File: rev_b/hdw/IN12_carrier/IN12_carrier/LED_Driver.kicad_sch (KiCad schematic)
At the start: 27 parts, among them U2101 LP5009

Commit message: lots of routing and design progress on IN12 carrier board
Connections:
- net +3V3 renamed +3.3V
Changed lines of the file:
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@@
     )
   )
-  (symbol (lib_id "Analog_Clock-rescue:+3.3V-power") (at 233.68 62.23 0) (unit 1)
+  (symbol (lib_id "power:+3.3V") (at 233.68 62.23 0) (unit 1)
     (in_bom yes) (on_board yes) (dnp no)
     (property "Reference" "#PWR01819" (at 233.68 66.04 0)
@@
     )
   )
-  (symbol (lib_id "Analog_Clock-rescue:+3.3V-power") (at 85.344 146.304 0) (unit 1)
+  (symbol (lib_id "power:+3.3V") (at 85.344 146.304 0) (unit 1)
     (in_bom yes) (on_board yes) (dnp no)
     (property "Reference" "#PWR?" (at 85.344 150.114 0)
@@
     )
   )
-  (symbol (lib_id "Analog_Clock-rescue:+3.3V-power") (at 104.394 146.304 0) (unit 1)
+  (symbol (lib_id "power:+3.3V") (at 104.394 146.304 0) (unit 1)
     (in_bom yes) (on_board yes) (dnp no)
     (property "Reference" "#PWR?" (at 104.394 150.114 0)
@@
     )
   )
-  (symbol (lib_id "Analog_Clock-rescue:+3.3V-power") (at 83.82 115.57 90) (unit 1)
+  (symbol (lib_id "power:+3.3V") (at 83.82 115.57 90) (unit 1)
     (in_bom yes) (on_board yes) (dnp no)
     (property "Reference" "#PWR02108" (at 87.63 115.57 0)
@@
     )
   )
-  (symbol (lib_id "Analog_Clock-rescue:+3.3V-power") (at 104.14 24.13 0) (unit 1)
+  (symbol (lib_id "power:+3.3V") (at 104.14 24.13 0) (unit 1)
     (in_bom yes) (on_board yes) (dnp no)
     (property "Reference" "#PWR?" (at 104.14 27.94 0)
@@
     )
   )
-  (symbol (lib_id "Analog_Clock-rescue:+3.3V-power") (at 93.98 100.33 0) (unit 1)
+  (symbol (lib_id "power:+3.3V") (at 93.98 100.33 0) (unit 1)
     (in_bom yes) (on_board yes) (dnp no)
     (property "Reference" "#PWR02108" (at 93.98 104.14 0)
@@
     )
   )
-  (symbol (lib_id "Analog_Clock-rescue:+3.3V-power") (at 154.94 29.21 0) (unit 1)
+  (symbol (lib_id "power:+3.3V") (at 154.94 29.21 0) (unit 1)
     (in_bom yes) (on_board yes) (dnp no)
     (property "Reference" "#PWR01819" (at 154.94 33.02 0)
@@
     )
   )
-  (symbol (lib_id "Analog_Clock-rescue:+3.3V-power") (at 233.68 29.21 0) (unit 1)
+  (symbol (lib_id "power:+3.3V") (at 233.68 29.21 0) (unit 1)
     (in_bom yes) (on_board yes) (dnp no)
     (property "Reference" "#PWR01819" (at 233.68 33.02 0)
@@
     )
   )
-  (symbol (lib_id "Analog_Clock-rescue:+3.3V-power") (at 93.98 161.29 0) (unit 1)
+  (symbol (lib_id "power:+3.3V") (at 93.98 161.29 0) (unit 1)
     (in_bom yes) (on_board yes) (dnp no)
     (property "Reference" "#PWR02108" (at 93.98 165.1 0)
@@
     )
   )
-  (symbol (lib_id "Analog_Clock-rescue:+3.3V-power") (at 194.31 62.23 0) (unit 1)
+  (symbol (lib_id "power:+3.3V") (at 194.31 62.23 0) (unit 1)
     (in_bom yes) (on_board yes) (dnp no)
     (property "Reference" "#PWR01819" (at 194.31 66.04 0)
@@
     )
   )
-  (symbol (lib_id "Analog_Clock-rescue:+3.3V-power") (at 93.98 39.37 0) (unit 1)
+  (symbol (lib_id "power:+3.3V") (at 93.98 39.37 0) (unit 1)
     (in_bom yes) (on_board yes) (dnp no)
     (property "Reference" "#PWR02108" (at 93.98 43.18 0)
@@
     )
   )
-  (symbol (lib_id "Analog_Clock-rescue:+3.3V-power") (at 85.344 85.344 0) (unit 1)
+  (symbol (lib_id "power:+3.3V") (at 85.344 85.344 0) (unit 1)
     (in_bom yes) (on_board yes) (dnp no)
     (property "Reference" "#PWR?" (at 85.344 89.154 0)
@@
     )
   )
-  (symbol (lib_id "Analog_Clock-rescue:+3.3V-power") (at 154.94 62.23 0) (unit 1)
+  (symbol (lib_id "power:+3.3V") (at 154.94 62.23 0) (unit 1)
     (in_bom yes) (on_board yes) (dnp no)
     (property "Reference" "#PWR01819" (at 154.94 66.04 0)
@@
     )
   )
-  (symbol (lib_id "Analog_Clock-rescue:+3.3V-power") (at 154.94 100.33 0) (unit 1)
+  (symbol (lib_id "power:+3.3V") (at 154.94 100.33 0) (unit 1)
     (in_bom yes) (on_board yes) (dnp no)
     (property "Reference" "#PWR01819" (at 154.94 104.14 0)
@@
     )
   )
-  (symbol (lib_id "Analog_Clock-rescue:+3.3V-power") (at 194.31 100.33 0) (unit 1)
+  (symbol (lib_id "power:+3.3V") (at 194.31 100.33 0) (unit 1)
     (in_bom yes) (on_board yes) (dnp no)
     (property "Reference" "#PWR01819" (at 194.31 104.14 0)
@@
     )
   )
-  (symbol (lib_id "Analog_Clock-rescue:+3.3V-power") (at 85.09 24.13 0) (unit 1)
+  (symbol (lib_id "power:+3.3V") (at 85.09 24.13 0) (unit 1)
     (in_bom yes) (on_board yes) (dnp no)
     (property "Reference" "#PWR?" (at 85.09 27.94 0)
@@
     )
   )
-  (symbol (lib_id "Analog_Clock-rescue:+3.3V-power") (at 83.82 179.07 90) (unit 1)
+  (symbol (lib_id "power:+3.3V") (at 83.82 179.07 90) (unit 1)
     (in_bom yes) (on_board yes) (dnp no)
     (property "Reference" "#PWR02108" (at 87.63 179.07 0)
@@
     )
   )
-  (symbol (lib_id "Analog_Clock-rescue:+3.3V-power") (at 194.31 29.21 0) (unit 1)
+  (symbol (lib_id "power:+3.3V") (at 194.31 29.21 0) (unit 1)
     (in_bom yes) (on_board yes) (dnp no)
     (property "Reference" "#PWR01819" (at 194.31 33.02 0)
@@
     )
   )
-  (symbol (lib_id "Analog_Clock-rescue:+3.3V-power") (at 104.394 85.344 0) (unit 1)
+  (symbol (lib_id "power:+3.3V") (at 104.394 85.344 0) (unit 1)
     (in_bom yes) (on_board yes) (dnp no)
     (property "Reference" "#PWR?" (at 104.394 89.154 0)

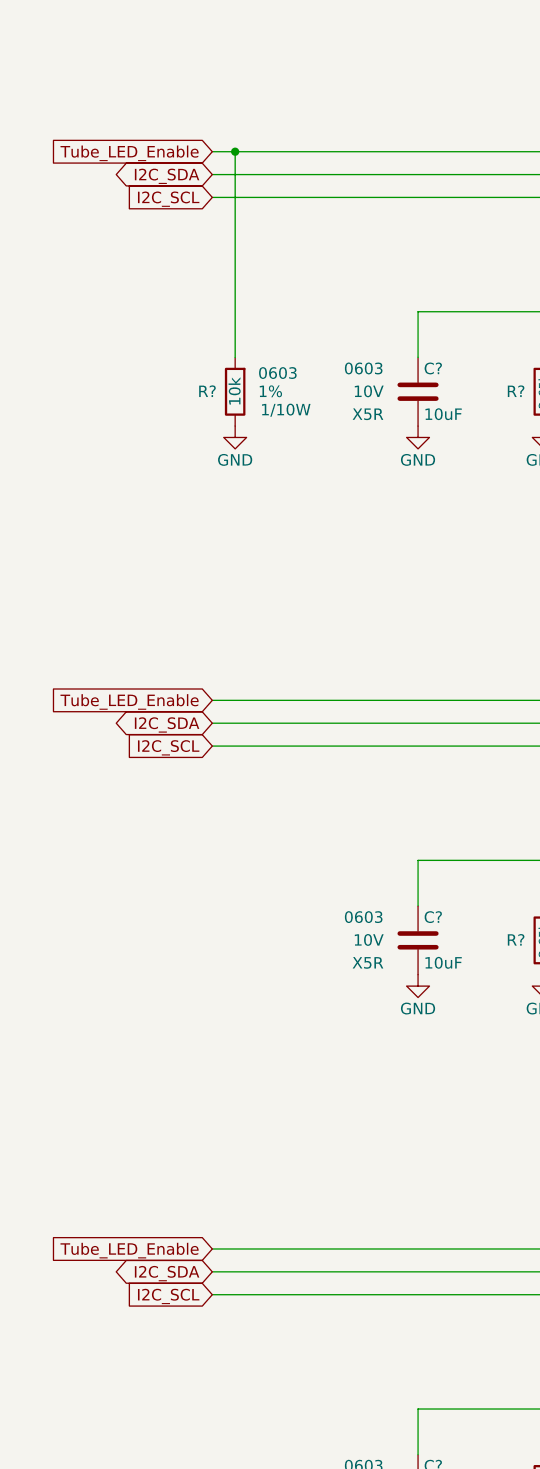
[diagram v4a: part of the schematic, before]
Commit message: got IN12 carrier board unconnects to 0
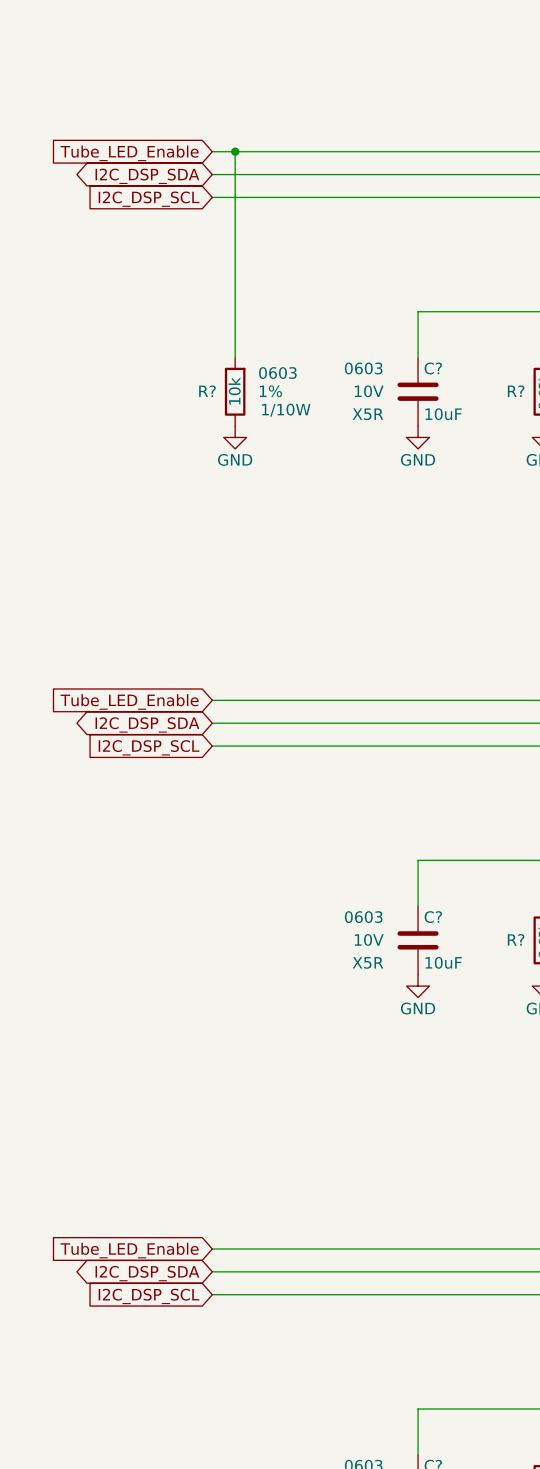
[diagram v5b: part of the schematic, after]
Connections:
- net I2C_SCL renamed I2C_DSP_SCL
- net I2C_SDA renamed I2C_DSP_SDA
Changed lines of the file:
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@@
     )
   )
-  (global_label "I2C_SCL" (shape input) (at 38.1 110.49 180)
+  (global_label "I2C_DSP_SCL" (shape input) (at 38.1 110.49 180)
     (effects (font (size 1.27 1.27)) (justify right))
     (property "Intersheetrefs" "${INTERSHEET_REFS}" (at 38.1 110.49 0)
@@
     )
   )
-  (global_label "I2C_SDA" (shape bidirectional) (at 38.1 46.99 180)
+  (global_label "I2C_DSP_SDA" (shape bidirectional) (at 38.1 46.99 180)
     (effects (font (size 1.27 1.27)) (justify right))
     (property "Intersheetrefs" "${INTERSHEET_REFS}" (at 38.1 46.99 0)
@@
     )
   )
-  (global_label "I2C_SDA" (shape bidirectional) (at 38.1 168.91 180)
+  (global_label "I2C_DSP_SDA" (shape bidirectional) (at 38.1 168.91 180)
     (effects (font (size 1.27 1.27)) (justify right))
     (property "Intersheetrefs" "${INTERSHEET_REFS}" (at 38.1 168.91 0)
@@
     )
   )
-  (global_label "I2C_SCL" (shape input) (at 38.1 49.53 180)
+  (global_label "I2C_DSP_SCL" (shape input) (at 38.1 49.53 180)
     (effects (font (size 1.27 1.27)) (justify right))
     (property "Intersheetrefs" "${INTERSHEET_REFS}" (at 38.1 49.53 0)
@@
     )
   )
-  (global_label "I2C_SDA" (shape bidirectional) (at 38.1 107.95 180)
+  (global_label "I2C_DSP_SDA" (shape bidirectional) (at 38.1 107.95 180)
     (effects (font (size 1.27 1.27)) (justify right))
     (property "Intersheetrefs" "${INTERSHEET_REFS}" (at 38.1 107.95 0)
@@
     )
   )
-  (global_label "I2C_SCL" (shape input) (at 38.1 171.45 180)
+  (global_label "I2C_DSP_SCL" (shape input) (at 38.1 171.45 180)
     (effects (font (size 1.27 1.27)) (justify right))
     (property "Intersheetrefs" "${INTERSHEET_REFS}" (at 38.1 171.45 0)

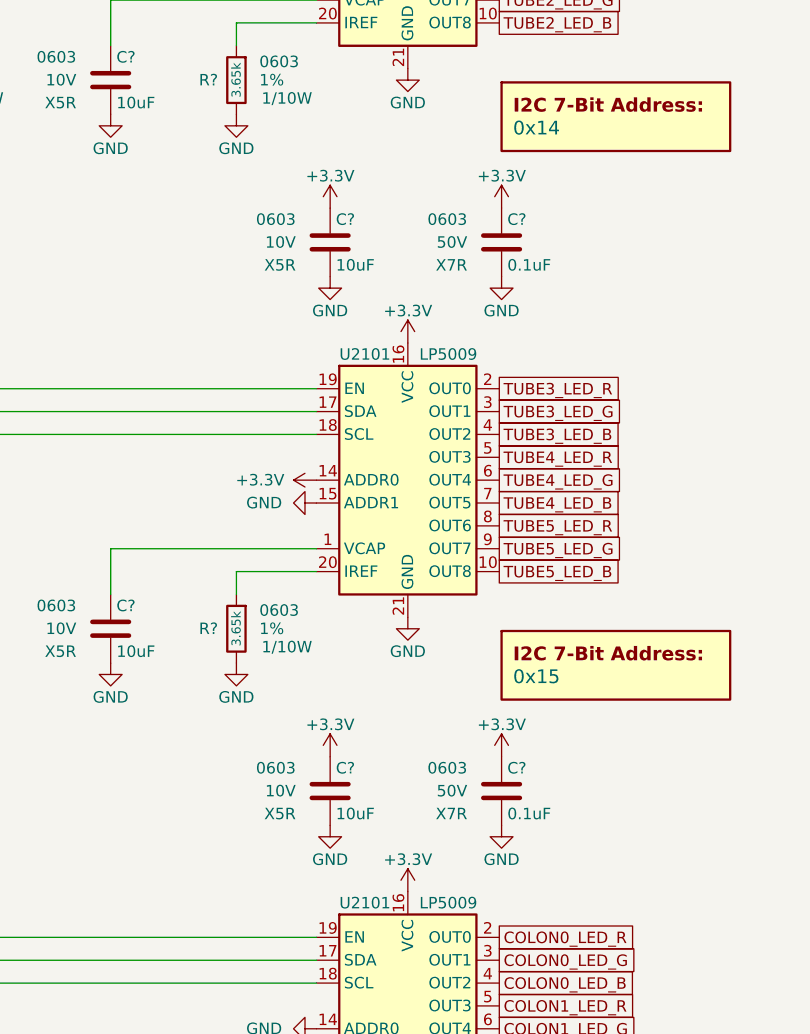
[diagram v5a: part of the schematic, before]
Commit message: added BOM for IN12 carrier, finished routing, some schematic tweaks, adjusted design rules for ERC
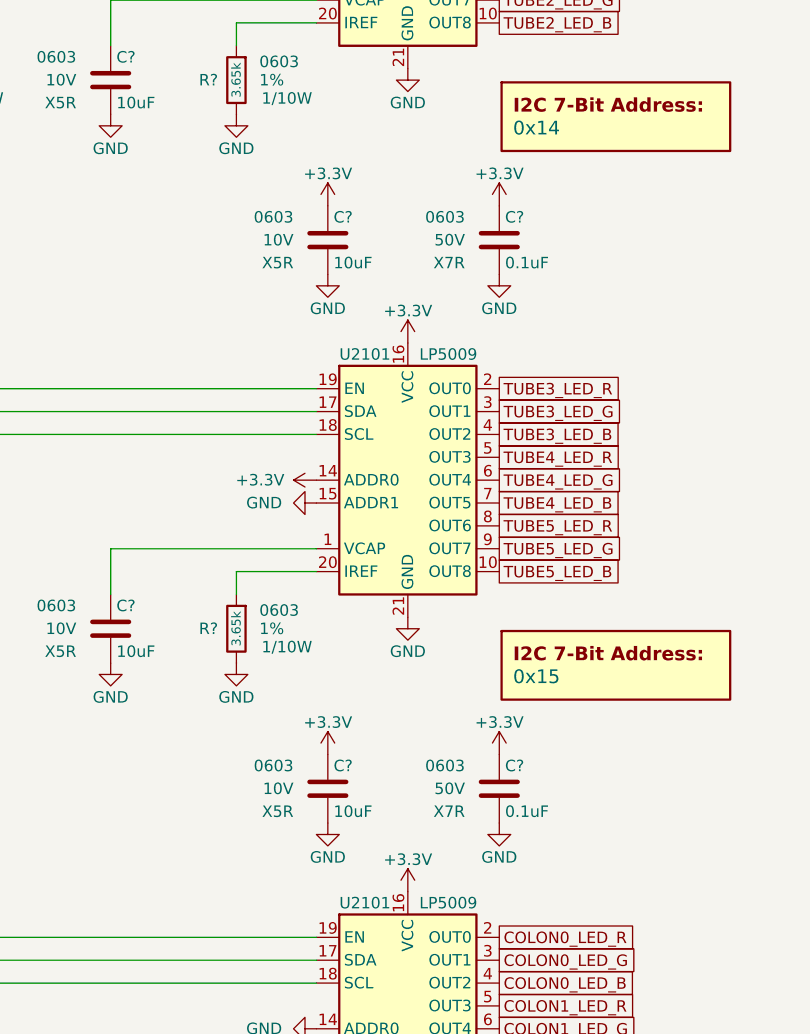
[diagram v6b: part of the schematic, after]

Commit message: assigned digikey pns to IN12 carrier board parts
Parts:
- C? (x3): Digi-Key PN (none) -> 1276-CL10B104KB8NNNLCT-ND
- C? (x6): Digi-Key PN (none) -> 1276-1871-1-ND
- R? (x3): Digi-Key PN (none) -> 541-3.65KHCT-ND
- R?: Digi-Key PN (none) -> 541-10.0KHCT-ND
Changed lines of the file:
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@@
       (effects (font (size 1.27 1.27)) (justify right))
     )
-    (property "Digi-Key PN" "" (at 4.826 263.652 0)
+    (property "Digi-Key PN" "1276-CL10B104KB8NNNLCT-ND" (at 4.826 263.652 0)
       (effects (font (size 1.27 1.27)) hide)
     )
@@
       (effects (font (size 1.27 1.27)) (justify right))
     )
-    (property "Digi-Key PN" "" (at 85.09 27.94 0)
+    (property "Digi-Key PN" "1276-1871-1-ND" (at 85.09 27.94 0)
       (effects (font (size 1.27 1.27)) hide)
     )
@@
       (effects (font (size 1.27 1.27)) (justify left))
     )
-    (property "Digi-Key PN" "" (at 74.93 132.08 0)
+    (property "Digi-Key PN" "541-3.65KHCT-ND" (at 74.93 132.08 0)
       (effects (font (size 1.27 1.27)) hide)
     )
@@
       (effects (font (size 1.27 1.27)) (justify right))
     )
-    (property "Digi-Key PN" "" (at 4.826 202.692 0)
+    (property "Digi-Key PN" "1276-CL10B104KB8NNNLCT-ND" (at 4.826 202.692 0)
       (effects (font (size 1.27 1.27)) hide)
     )
@@
       (effects (font (size 1.27 1.27)) (justify left))
     )
-    (property "Digi-Key PN" "" (at 74.93 71.12 0)
+    (property "Digi-Key PN" "541-3.65KHCT-ND" (at 74.93 71.12 0)
       (effects (font (size 1.27 1.27)) hide)
     )
@@
       (effects (font (size 1.27 1.27)) (justify right))
     )
-    (property "Digi-Key PN" "" (at 4.826 324.612 0)
+    (property "Digi-Key PN" "1276-CL10B104KB8NNNLCT-ND" (at 4.826 324.612 0)
       (effects (font (size 1.27 1.27)) hide)
     )
@@
       (effects (font (size 1.27 1.27)) (justify right))
     )
-    (property "Digi-Key PN" "" (at 60.96 71.12 0)
+    (property "Digi-Key PN" "1276-1871-1-ND" (at 60.96 71.12 0)
       (effects (font (size 1.27 1.27)) hide)
     )
@@
       (effects (font (size 1.27 1.27)) (justify left))
     )
-    (property "Digi-Key PN" "" (at 74.93 193.04 0)
+    (property "Digi-Key PN" "541-3.65KHCT-ND" (at 74.93 193.04 0)
       (effects (font (size 1.27 1.27)) hide)
     )
@@
       (effects (font (size 1.27 1.27)) (justify right))
     )
-    (property "Digi-Key PN" "" (at 85.09 149.86 0)
+    (property "Digi-Key PN" "1276-1871-1-ND" (at 85.09 149.86 0)
       (effects (font (size 1.27 1.27)) hide)
     )
@@
       (effects (font (size 1.27 1.27)) (justify right))
     )
-    (property "Digi-Key PN" "" (at 60.96 132.08 0)
+    (property "Digi-Key PN" "1276-1871-1-ND" (at 60.96 132.08 0)
       (effects (font (size 1.27 1.27)) hide)
     )
@@
       (effects (font (size 1.27 1.27)) (justify right))
     )
-    (property "Digi-Key PN" "" (at 85.09 88.9 0)
+    (property "Digi-Key PN" "1276-1871-1-ND" (at 85.09 88.9 0)
       (effects (font (size 1.27 1.27)) hide)
     )
@@
       (effects (font (size 1.27 1.27)) (justify left))
     )
-    (property "Digi-Key PN" "" (at 48.26 60.96 0)
+    (property "Digi-Key PN" "541-10.0KHCT-ND" (at 48.26 60.96 0)
       (effects (font (size 1.524 1.524)) hide)
     )
@@
       (effects (font (size 1.27 1.27)) (justify right))
     )
-    (property "Digi-Key PN" "" (at 60.96 193.04 0)
-      (effects (font (size 1.27 1.27)) hide)
-    )
+    (property "Digi-Key PN" "1276-1871-1-ND" (at 60.96 193.04 0)
+      (effects (font (size 1.27 1.27)) hide)
+    )
